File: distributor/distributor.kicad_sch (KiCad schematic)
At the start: 10 parts, among them J1 Cerebellum, J10 CAN FD, J2 Cerebrum, J3 XT60PW-M, J4 CAN FD, J5 LegL, J6 ArmL, J7 LegR, J8 ArmR, J9 XT60PW-M

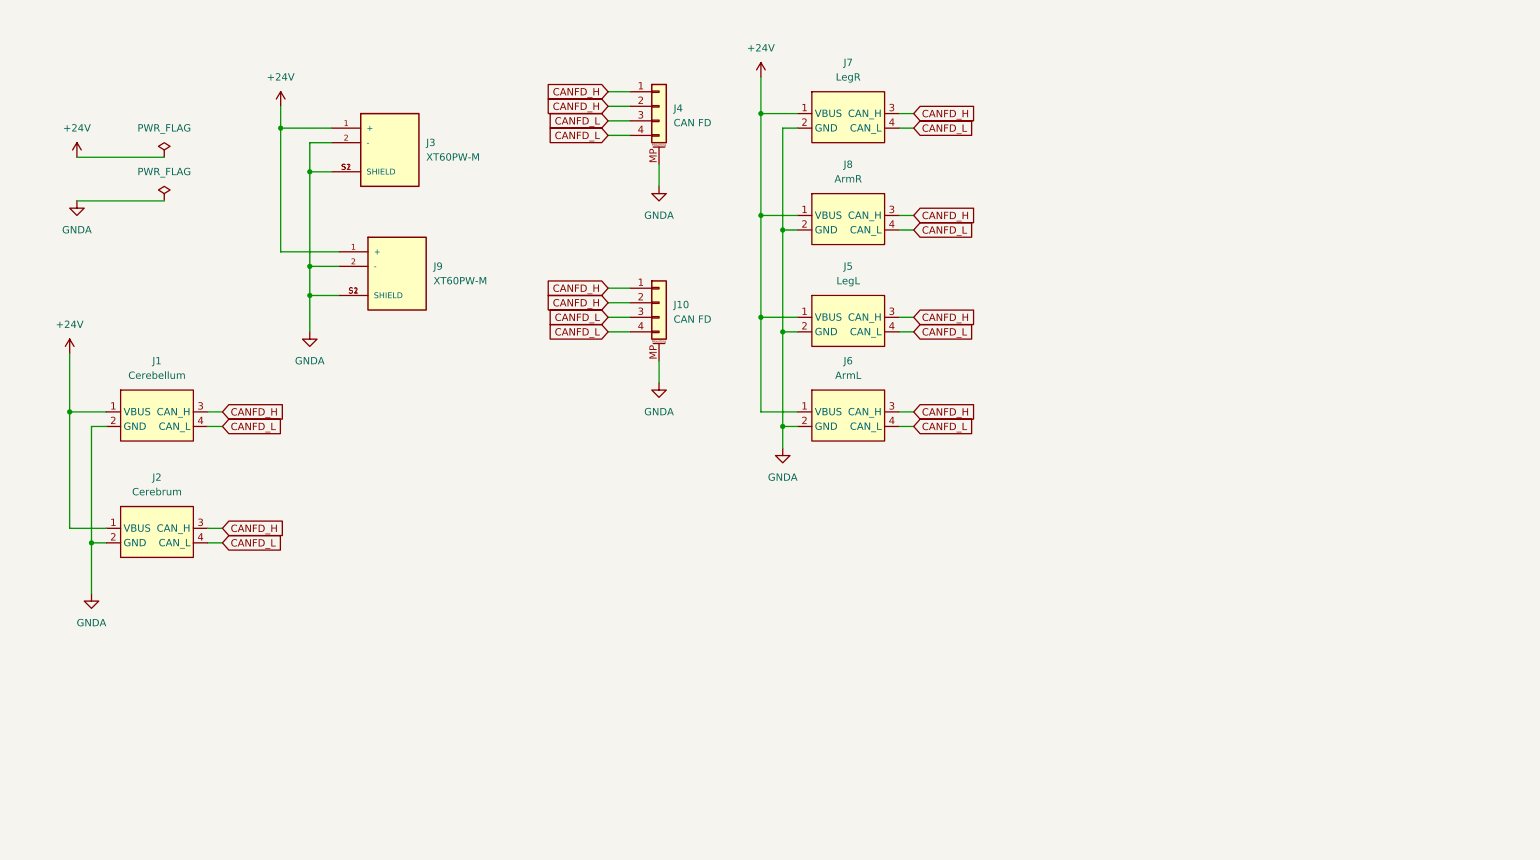
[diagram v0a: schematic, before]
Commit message: [Modify] Remove XT30(2+2), replaced by XT30 + GH 2pins
XT30(2+2) is not as robust as expected, so I replace all ports by XT30 and JST GH 1.25mm 2pin.
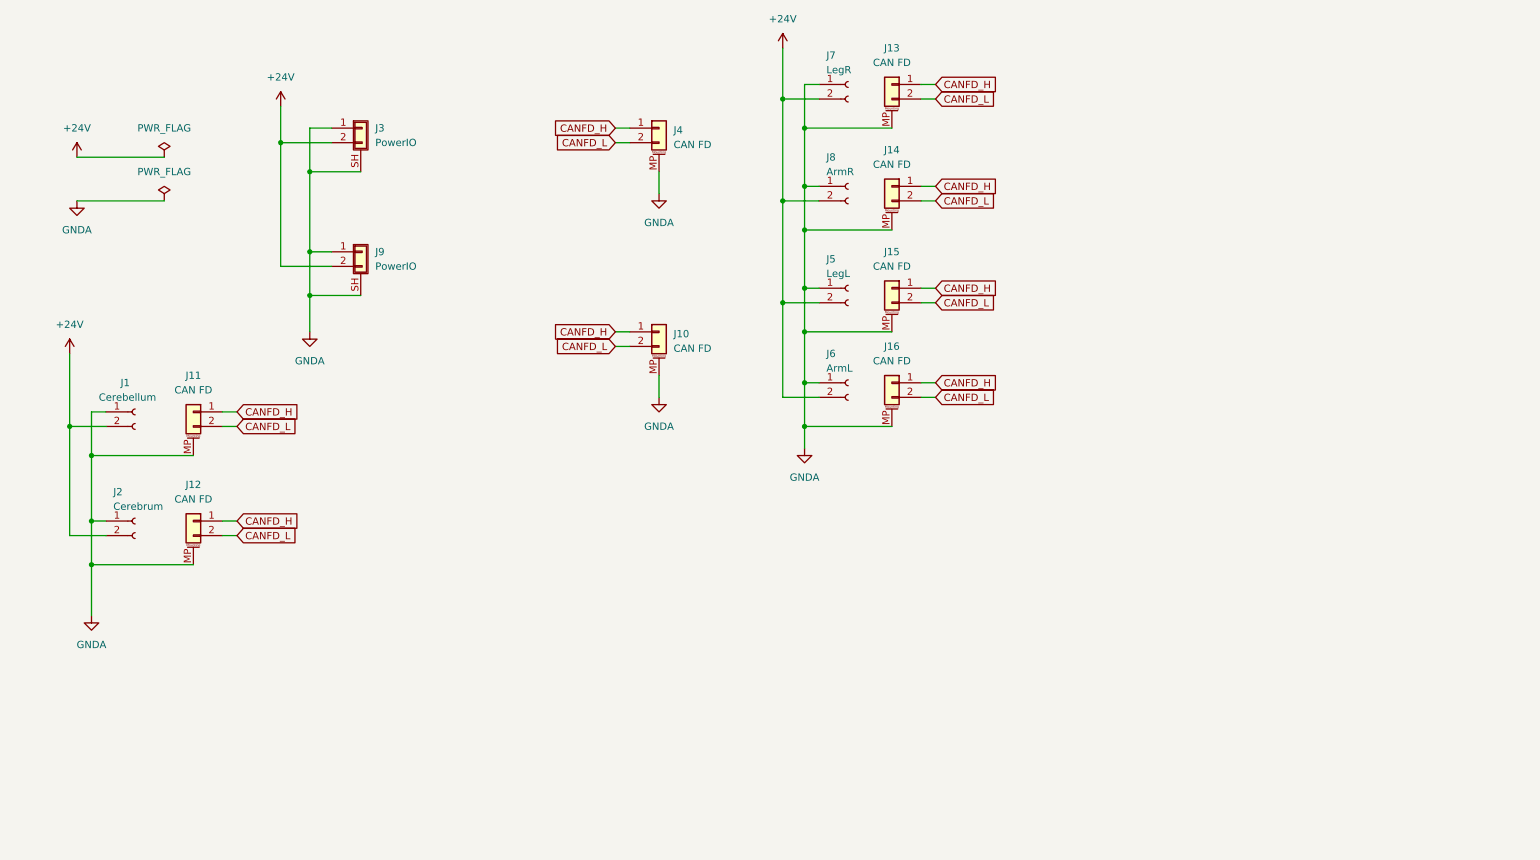
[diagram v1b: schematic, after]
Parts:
- removed J1: Cerebellum, Rolling_Custom:XT30PW(2+2), symbol Rolling_Custom:XT30PW(2+2)
- removed J10, J4: CAN FD, Connector_JST:JST_GH_SM04B-GHS-TB_1x04-1MP_P1.25mm_Horizontal, symbol Connector_Generic_MountingPin:Conn_01x04_MountingPin
- removed J2: Cerebrum, Rolling_Custom:XT30PW(2+2), symbol Rolling_Custom:XT30PW(2+2)
- removed J3, J9: XT60PW-M, Rolling_Custom:AMASS_XT60PW-M, symbol Rolling_Custom:XT60PW-M
- removed J5: LegL, Rolling_Custom:XT30PW(2+2), symbol Rolling_Custom:XT30PW(2+2)
- removed J6: ArmL, Rolling_Custom:XT30PW(2+2), symbol Rolling_Custom:XT30PW(2+2)
- removed J7: LegR, Rolling_Custom:XT30PW(2+2), symbol Rolling_Custom:XT30PW(2+2)
- removed J8: ArmR, Rolling_Custom:XT30PW(2+2), symbol Rolling_Custom:XT30PW(2+2)
- added J1: Cerebellum, Connector_AMASS:AMASS_XT30PW-F_1x02_P2.50mm_Horizontal, symbol Connector:Conn_01x02_Female
- added J10, J11, J12, J13, J14, J15, J16, J4: CAN FD, Connector_JST:JST_GH_SM02B-GHS-TB_1x02-1MP_P1.25mm_Horizontal, symbol Connector_Generic_MountingPin:Conn_01x02_MountingPin
- added J2: Cerebrum, Connector_AMASS:AMASS_XT30PW-F_1x02_P2.50mm_Horizontal, symbol Connector:Conn_01x02_Female
- added J3, J9: PowerIO, Rolling_Custom:AMASS_XT60PW-M, symbol Connector_Generic_Shielded:Conn_01x02_Shielded
- added J5: LegL, Connector_AMASS:AMASS_XT30PW-F_1x02_P2.50mm_Horizontal, symbol Connector:Conn_01x02_Female
- added J6: ArmL, Connector_AMASS:AMASS_XT30PW-F_1x02_P2.50mm_Horizontal, symbol Connector:Conn_01x02_Female
- added J7: LegR, Connector_AMASS:AMASS_XT30PW-F_1x02_P2.50mm_Horizontal, symbol Connector:Conn_01x02_Female
- added J8: ArmR, Connector_AMASS:AMASS_XT30PW-F_1x02_P2.50mm_Horizontal, symbol Connector:Conn_01x02_Female
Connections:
- net +24V: now also J1.2 (Pin_2), J2.2 (Pin_2), J3.2 (Pin_2), J5.2 (Pin_2), J6.2 (Pin_2), J7.2 (Pin_2), J8.2 (Pin_2), J9.2 (Pin_2)
- net CANFD_H: now also J10.1 (Pin_1), J11.1 (Pin_1), J12.1 (Pin_1), J13.1 (Pin_1), J14.1 (Pin_1), J15.1 (Pin_1), J16.1 (Pin_1), J4.1 (Pin_1)
- net CANFD_L: now also J10.2 (Pin_2), J11.2 (Pin_2), J12.2 (Pin_2), J13.2 (Pin_2), J14.2 (Pin_2), J15.2 (Pin_2), J16.2 (Pin_2), J4.2 (Pin_2)
- net GNDA: now also J1.1 (Pin_1), J10.MP (MountPin), J11.MP (MountPin), J12.MP (MountPin), J13.MP (MountPin), J14.MP (MountPin), J15.MP (MountPin), J16.MP (MountPin), J2.1 (Pin_1), J3.1 (Pin_1), J3.SH (Shield), J4.MP (MountPin), J5.1 (Pin_1), J6.1 (Pin_1), J7.1 (Pin_1), J8.1 (Pin_1), J9.1 (Pin_1), J9.SH (Shield)

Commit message: [New] Add 24V to 5V converter to distributor
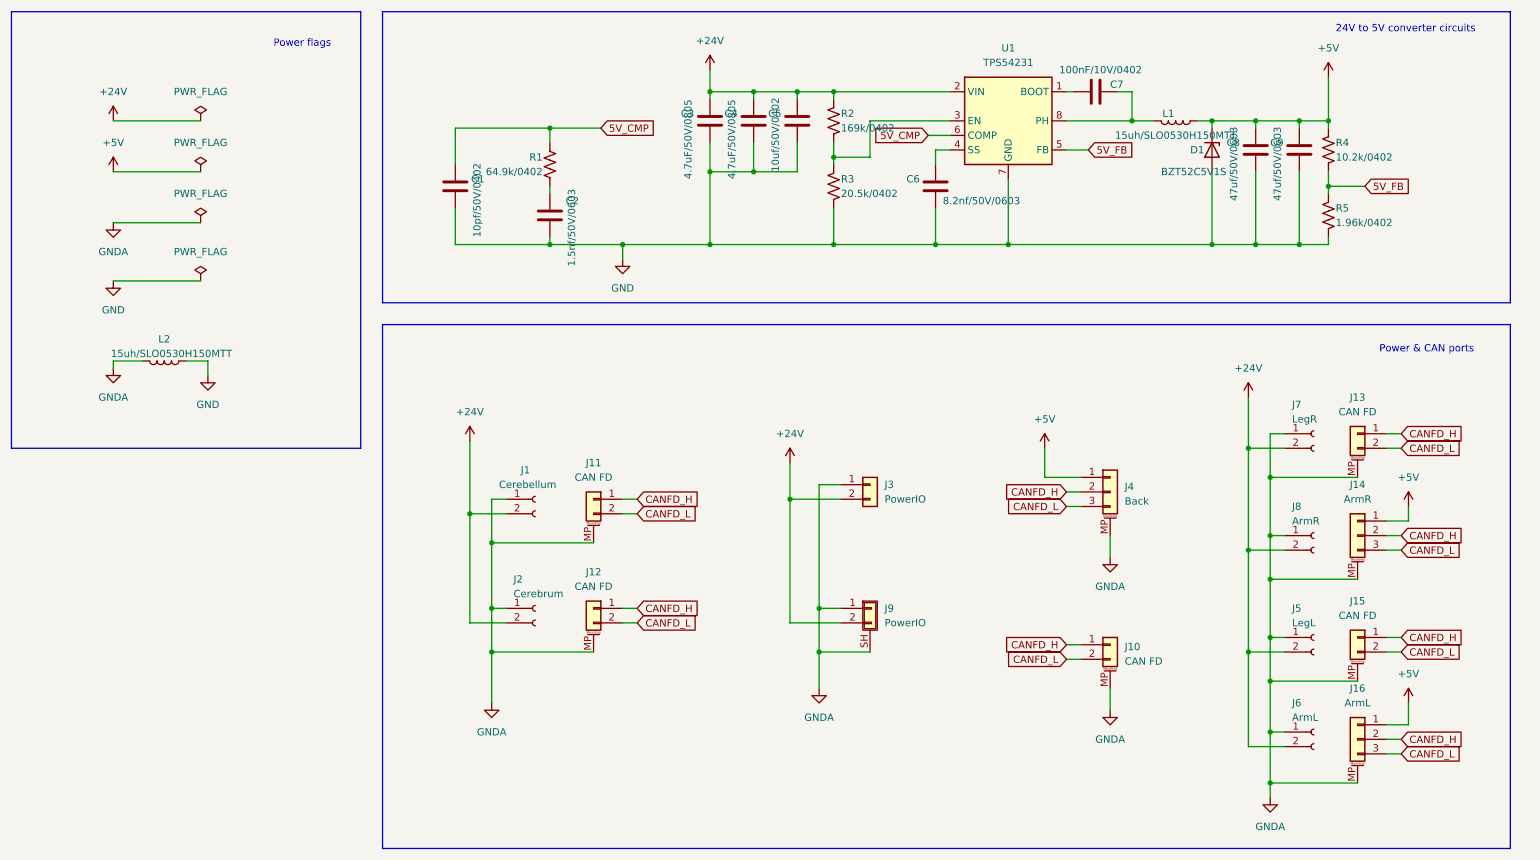
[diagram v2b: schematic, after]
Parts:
- removed J14, J16, J4: CAN FD, Connector_JST:JST_GH_SM02B-GHS-TB_1x02-1MP_P1.25mm_Horizontal, symbol Connector_Generic_MountingPin:Conn_01x02_MountingPin
- removed J3: PowerIO, Rolling_Custom:AMASS_XT60PW-M, symbol Connector_Generic_Shielded:Conn_01x02_Shielded
- added C1: 10pf/50V/0402, Capacitor_SMD:C_0402_1005Metric, symbol Device:C
- added C2: 1.5nf/50V/0603, Capacitor_SMD:C_0603_1608Metric, symbol Device:C
- added C3, C4: 4.7uF/50V/0805, Capacitor_SMD:C_0805_2012Metric, symbol Device:C
- added C5: 10uf/50V/0402, Capacitor_SMD:C_0402_1005Metric, symbol Device:C
- added C6: 8.2nf/50V/0603, Capacitor_SMD:C_0603_1608Metric, symbol Device:C
- added C7: 100nF/10V/0402, Capacitor_SMD:C_0402_1005Metric, symbol Device:C
- added C8, C9: 47uf/50V/0603, Capacitor_SMD:C_0603_1608Metric, symbol Device:C
- added D1: BZT52C5V1S, Diode_SMD:D_SOD-323, symbol Diode:BZT52Bxx
- added J14: ArmR, Connector_JST:JST_GH_SM03B-GHS-TB_1x03-1MP_P1.25mm_Horizontal, symbol Connector_Generic_MountingPin:Conn_01x03_MountingPin
- added J16: ArmL, Connector_JST:JST_GH_SM03B-GHS-TB_1x03-1MP_P1.25mm_Horizontal, symbol Connector_Generic_MountingPin:Conn_01x03_MountingPin
- added J3: PowerIO, Connector_AMASS:AMASS_XT30PW-M_1x02_P2.50mm_Horizontal, symbol Connector_Generic:Conn_01x02
- added J4: Back, Connector_JST:JST_GH_SM03B-GHS-TB_1x03-1MP_P1.25mm_Horizontal, symbol Connector_Generic_MountingPin:Conn_01x03_MountingPin
- added L1, L2: 15uh/SLO0530H150MTT, Inductor_SMD:L_Sunlord_MWSA0518_5.4x5.2mm, symbol Device:L
- added R1: 64.9k/0402, Resistor_SMD:R_0402_1005Metric, symbol Device:R_US
- added R2: 169k/0402, Resistor_SMD:R_0402_1005Metric, symbol Device:R_US
- added R3: 20.5k/0402, Resistor_SMD:R_0402_1005Metric, symbol Device:R_US
- added R4: 10.2k/0402, Resistor_SMD:R_0402_1005Metric, symbol Device:R_US
- added R5: 1.96k/0402, Resistor_SMD:R_0402_1005Metric, symbol Device:R_US
- added U1: TPS54231, Package_SO:SOIC-8_3.9x4.9mm_P1.27mm, symbol Regulator_Switching:TPS54233
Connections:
- net +24V: now also C3.1, C4.1, C5.1, J3.2 (Pin_2), R2.1, U1.2 (VIN)
- net CANFD_H: now also J14.2 (Pin_2), J16.2 (Pin_2), J4.2 (Pin_2)
- net CANFD_L: now also J14.3 (Pin_3), J16.3 (Pin_3), J4.3 (Pin_3)
- net GNDA: now also J14.MP (MountPin), J16.MP (MountPin), J3.1 (Pin_1), J4.MP (MountPin), L2.2
- new net: R2.2, R3.1, U1.3 (EN)
- new net: C7.1, L1.2, U1.8 (PH)
- new net: C7.2, U1.1 (BOOT)
- new net: C2.1, R1.2
- new net: C6.1, U1.4 (SS)
- new net +5V: C8.1, C9.1, D1.1 (K), J14.1 (Pin_1), J16.1 (Pin_1), J4.1 (Pin_1), L1.1, R4.1
- new net 5V_CMP: C1.1, R1.1, U1.6 (COMP)
- new net 5V_FB: R4.2, R5.1, U1.5 (FB)
- new net GND: C1.2, C2.2, C3.2, C4.2, C5.2, C6.2, C8.2, C9.2, D1.2 (A), L2.1, R3.2, R5.2, U1.7 (GND)
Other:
- note added: "24V to 5V converter circuits"
- note added: "Power & CAN ports"
- note added: "Power flags"
- moved on the sheet: J1, J10, J11, J12, J13, J15, J2, J5, J6, J7, J8, J9

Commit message: [New] Release all board 3D models
* All files are in folder "steps".
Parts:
- J1, J2, J5, J6, J7, J8: footprint Connector_AMASS:AMASS_XT30PW-F_1x02_P2.50mm_Horizontal -> Connector_AMASS:AMASS_XT30PW-M_1x02_P2.50mm_Horizontal
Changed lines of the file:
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@@
       (effects (font (size 1.27 1.27)) (justify left))
     )
-    (property "Footprint" "Connector_AMASS:AMASS_XT30PW-F_1x02_P2.50mm_Horizontal" (id 2) (at 109.22 101.6 0)
+    (property "Footprint" "Connector_AMASS:AMASS_XT30PW-M_1x02_P2.50mm_Horizontal" (id 2) (at 109.22 101.6 0)
       (effects (font (size 1.27 1.27)) hide)
     )
@@
       (effects (font (size 1.27 1.27)) (justify left))
     )
-    (property "Footprint" "Connector_AMASS:AMASS_XT30PW-F_1x02_P2.50mm_Horizontal" (id 2) (at 245.11 125.73 0)
+    (property "Footprint" "Connector_AMASS:AMASS_XT30PW-M_1x02_P2.50mm_Horizontal" (id 2) (at 245.11 125.73 0)
       (effects (font (size 1.27 1.27)) hide)
     )
@@
       (effects (font (size 1.27 1.27)) (justify left))
     )
-    (property "Footprint" "Connector_AMASS:AMASS_XT30PW-F_1x02_P2.50mm_Horizontal" (id 2) (at 245.11 142.24 0)
+    (property "Footprint" "Connector_AMASS:AMASS_XT30PW-M_1x02_P2.50mm_Horizontal" (id 2) (at 245.11 142.24 0)
       (effects (font (size 1.27 1.27)) hide)
     )
@@
       (effects (font (size 1.27 1.27)) (justify left))
     )
-    (property "Footprint" "Connector_AMASS:AMASS_XT30PW-F_1x02_P2.50mm_Horizontal" (id 2) (at 245.11 90.17 0)
+    (property "Footprint" "Connector_AMASS:AMASS_XT30PW-M_1x02_P2.50mm_Horizontal" (id 2) (at 245.11 90.17 0)
       (effects (font (size 1.27 1.27)) hide)
     )
@@
       (effects (font (size 1.27 1.27)) (justify left))
     )
-    (property "Footprint" "Connector_AMASS:AMASS_XT30PW-F_1x02_P2.50mm_Horizontal" (id 2) (at 245.11 107.95 0)
+    (property "Footprint" "Connector_AMASS:AMASS_XT30PW-M_1x02_P2.50mm_Horizontal" (id 2) (at 245.11 107.95 0)
       (effects (font (size 1.27 1.27)) hide)
     )
@@
       (effects (font (size 1.27 1.27)) (justify left))
     )
-    (property "Footprint" "Connector_AMASS:AMASS_XT30PW-F_1x02_P2.50mm_Horizontal" (id 2) (at 109.22 120.65 0)
+    (property "Footprint" "Connector_AMASS:AMASS_XT30PW-M_1x02_P2.50mm_Horizontal" (id 2) (at 109.22 120.65 0)
       (effects (font (size 1.27 1.27)) hide)
     )
@@
     )
     (path "/115f2e1f-72cb-4cdb-b7af-b779ff7e41e0"
-      (reference "J1") (unit 1) (value "Cerebellum") (footprint "Connector_AMASS:AMASS_XT30PW-F_1x02_P2.50mm_Horizontal")
+      (reference "J1") (unit 1) (value "Cerebellum") (footprint "Connector_AMASS:AMASS_XT30PW-M_1x02_P2.50mm_Horizontal")
     )
     (path "/cb359a3e-d291-4a71-85b6-7f63dfd153bc"
-      (reference "J2") (unit 1) (value "Cerebrum") (footprint "Connector_AMASS:AMASS_XT30PW-F_1x02_P2.50mm_Horizontal")
+      (reference "J2") (unit 1) (value "Cerebrum") (footprint "Connector_AMASS:AMASS_XT30PW-M_1x02_P2.50mm_Horizontal")
     )
     (path "/f172c2a5-8237-40ee-b30c-4d728a071ffd"
@@
     )
     (path "/2a94316c-a232-40d0-9487-982903bcadcb"
-      (reference "J5") (unit 1) (value "LegL") (footprint "Connector_AMASS:AMASS_XT30PW-F_1x02_P2.50mm_Horizontal")
+      (reference "J5") (unit 1) (value "LegL") (footprint "Connector_AMASS:AMASS_XT30PW-M_1x02_P2.50mm_Horizontal")
     )
     (path "/81e1012f-fb62-4baf-8def-e42753269c68"
-      (reference "J6") (unit 1) (value "ArmL") (footprint "Connector_AMASS:AMASS_XT30PW-F_1x02_P2.50mm_Horizontal")
+      (reference "J6") (unit 1) (value "ArmL") (footprint "Connector_AMASS:AMASS_XT30PW-M_1x02_P2.50mm_Horizontal")
     )
     (path "/8314c951-2351-455f-9fa6-57685c9d2ac9"
-      (reference "J7") (unit 1) (value "LegR") (footprint "Connector_AMASS:AMASS_XT30PW-F_1x02_P2.50mm_Horizontal")
+      (reference "J7") (unit 1) (value "LegR") (footprint "Connector_AMASS:AMASS_XT30PW-M_1x02_P2.50mm_Horizontal")
     )
     (path "/ad74628d-9044-4ac8-8bc3-ebadcb864e01"
-      (reference "J8") (unit 1) (value "ArmR") (footprint "Connector_AMASS:AMASS_XT30PW-F_1x02_P2.50mm_Horizontal")
+      (reference "J8") (unit 1) (value "ArmR") (footprint "Connector_AMASS:AMASS_XT30PW-M_1x02_P2.50mm_Horizontal")
     )
     (path "/d04c7014-c40a-4aab-8464-ab8a978dba9f"

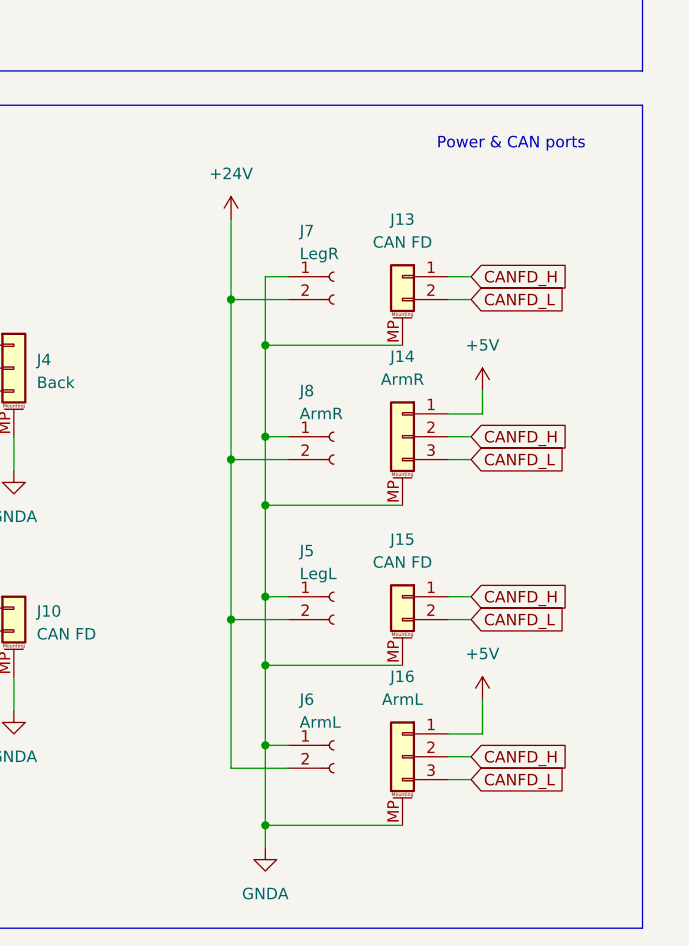
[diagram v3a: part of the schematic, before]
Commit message: [Fix] Correct mounting hole positions
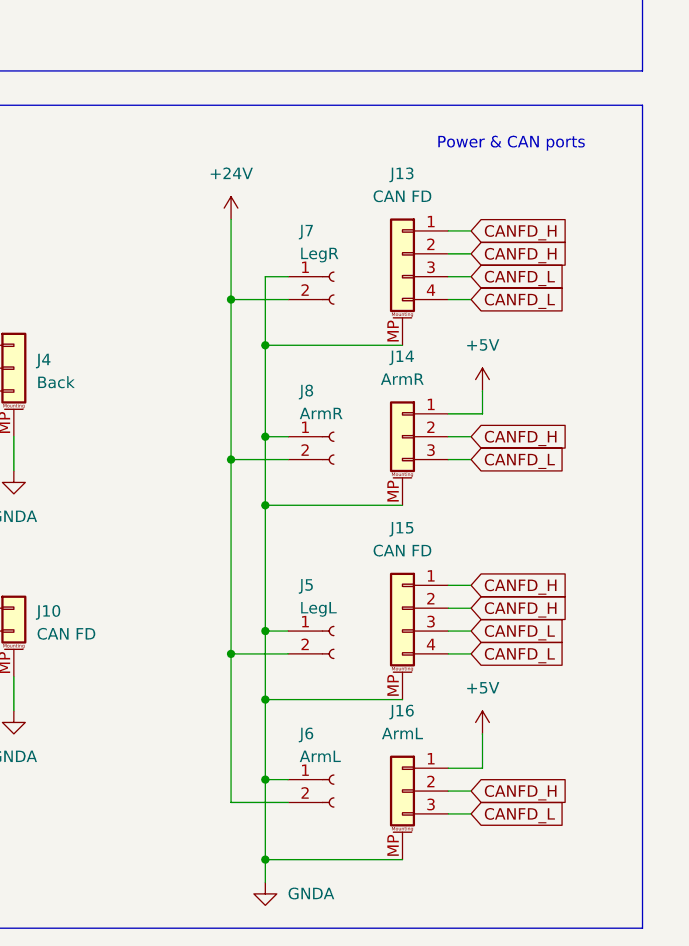
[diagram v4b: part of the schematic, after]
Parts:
- removed J13, J15: CAN FD, Connector_JST:JST_GH_SM02B-GHS-TB_1x02-1MP_P1.25mm_Horizontal, symbol Connector_Generic_MountingPin:Conn_01x02_MountingPin
- added J13, J15: CAN FD, Connector_JST:JST_GH_SM04B-GHS-TB_1x04-1MP_P1.25mm_Horizontal, symbol Connector_Generic_MountingPin:Conn_01x04_MountingPin
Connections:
- net CANFD_H: now also J13.1 (Pin_1), J13.2 (Pin_2), J15.1 (Pin_1), J15.2 (Pin_2)
- net CANFD_L: now also J13.3 (Pin_3), J13.4 (Pin_4), J15.3 (Pin_3), J15.4 (Pin_4)
- net GNDA: now also J13.MP (MountPin), J15.MP (MountPin)
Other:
- moved on the sheet: J16, J5, J6
